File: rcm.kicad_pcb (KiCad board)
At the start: 2 copper layers, 100 x 100 mm, 158 parts, among them Y1 8MHz, Y2 32.768kHz

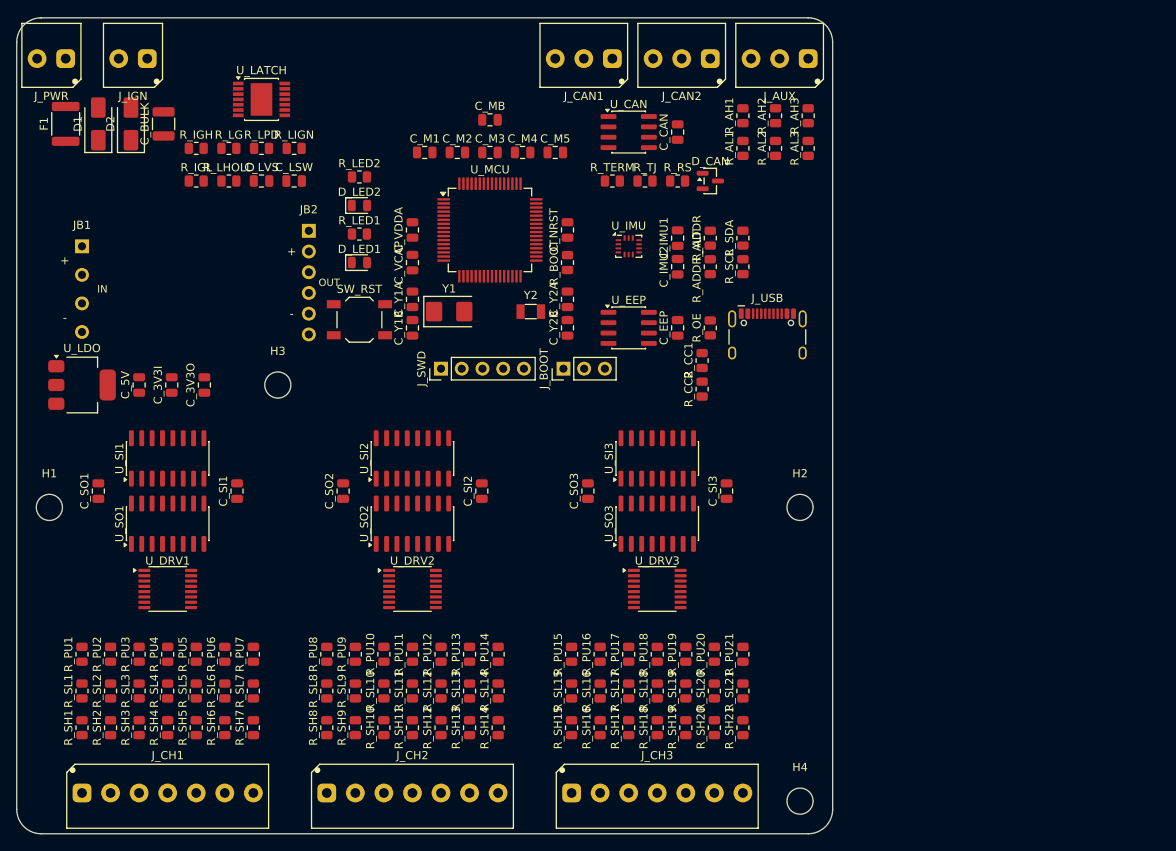
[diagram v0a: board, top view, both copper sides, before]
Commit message: rcm: reshape the board to 140x70 to match the keypad button panel
The panel is 8 momentary switches in 2 rows of 4 at 35mm each, so the board is
now 140 x 70mm. That is 98cm2 against the previous 100 x 100mm draft's 100cm2 -
the same area reshaped rather than a resize, so nothing was traded away for it.

A 70mm-tall board cannot take the old 46mm channel tiles, so each tile's driver,
both shift registers and their decoupling now sit in ONE row instead of a
column: 31mm of tile height, spending the width the wider board has. The north
half was rebuilt across the full 140mm.

Two bugs found on the way, both worth remembering:

- expand_placement pairs members[i] with refs[i]. Reordering the member offsets
  without reordering the ref list put U_SI in C_SO's slot on all three tiles. It
  only surfaced because those two collided; a reorder landing parts somewhere
  legal would have passed every check and still been wrong.
- The buck module body has no courtyard by design, so the placement lint is
  blind to it. gen_plan.py now hard-asserts the area is clear, and that assert
  immediately caught both status LEDs and a resistor underneath the module after
  the reshape - with the lint reporting 0 errors.

Placement lint 0/0, board DRC 0 errors. The 111 remaining warnings are all
silkscreen and get cleaned up in the dedicated pass at the end.

Co-Authored-By: Claude Opus 5 <noreply@anthropic.com>
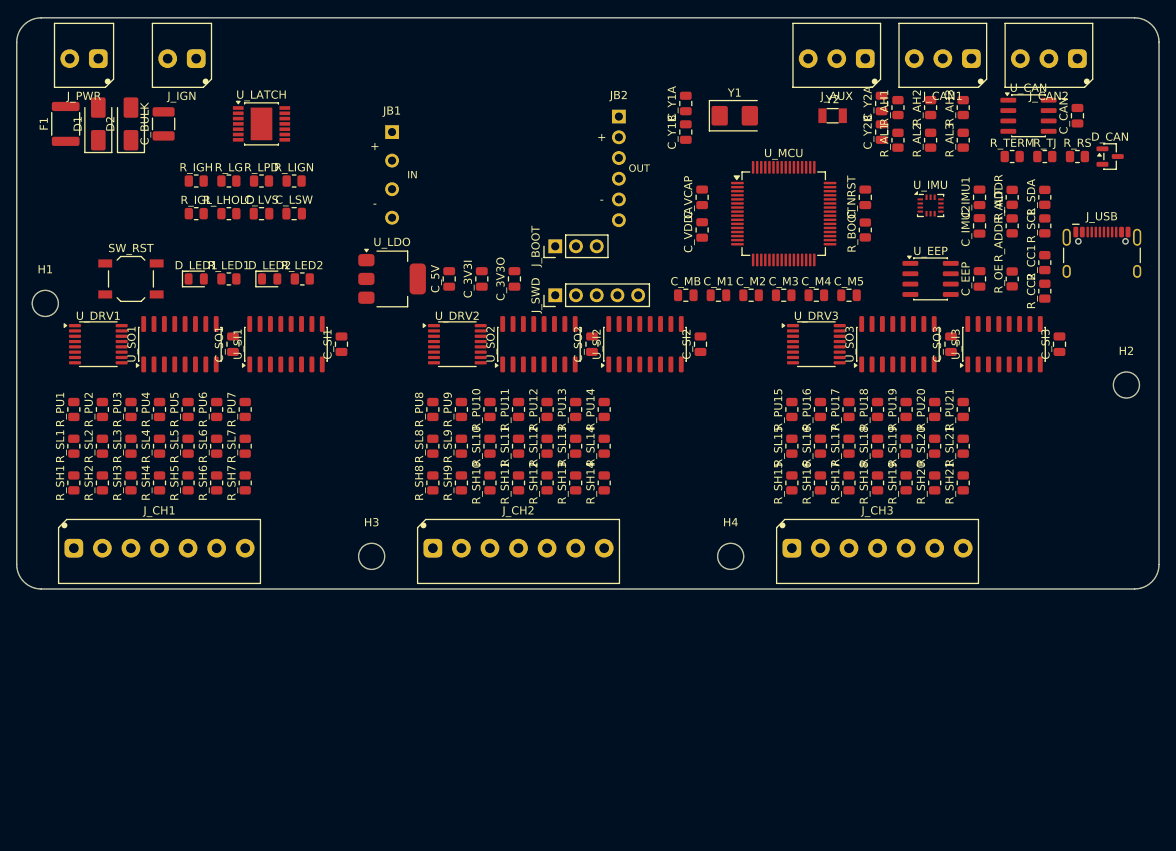
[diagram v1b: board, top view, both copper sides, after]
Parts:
- moved D_CAN 49.1 mm to (134.0, 17.0)
- moved R_RS 49.1 mm to (130.0, 17.0)
- moved R_TERM 49.1 mm to (122.0, 17.0)
- moved R_TJ 49.1 mm to (126.0, 17.0)
- moved C_CAN 49.0 mm to (130.0, 12.0)
- moved U_CAN 49.0 mm to (124.0, 12.0)
- moved C_SO3 48.0 mm to (114.5, 40.0)
- moved C_Y2A 45.4 mm to (106.0, 10.5)
- moved C_Y2B 45.4 mm to (106.0, 14.0)
- moved J_CAN2 45.0 mm to (130.0, 5.00)
- moved U_SI3 44.7 mm to (121.0, 40.0)
- moved C_SI3 44.6 mm to (127.8, 40.0)
- moved Y2 44.1 mm to (100.0, 12.0)
- moved J_CAN1 44.0 mm to (117.0, 5.00)
- moved R_CC1 43.7 mm to (126.0, 30.0)
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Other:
- board size 100 x 100 mm -> 140 x 70 mm

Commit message: rcm: reverse the 595 data chain and give the mounting holes washer clearance
Reviewing the rendered board, the shift-register data line entered at the tile
FURTHEST from the MCU - a ~74mm haul across the board before the chain doubled
back east past the MCU. Reversed so it enters at the nearest tile and ripples
away. Sets the bit order: first byte out lands in U_SO1 (channels 1-7).

The four mounting holes all sat 3.5-4.0mm from a board edge, which is exactly
the radius of an M3 washer - it would have overhung. Moved to 5mm+ and lifted
the two bottom holes clear of the terminal-block row.

Schematic ERC 0 and round-trip MATCH; placement lint 0/0; board DRC 0 errors.

Co-Authored-By: Claude Opus 5 <noreply@anthropic.com>
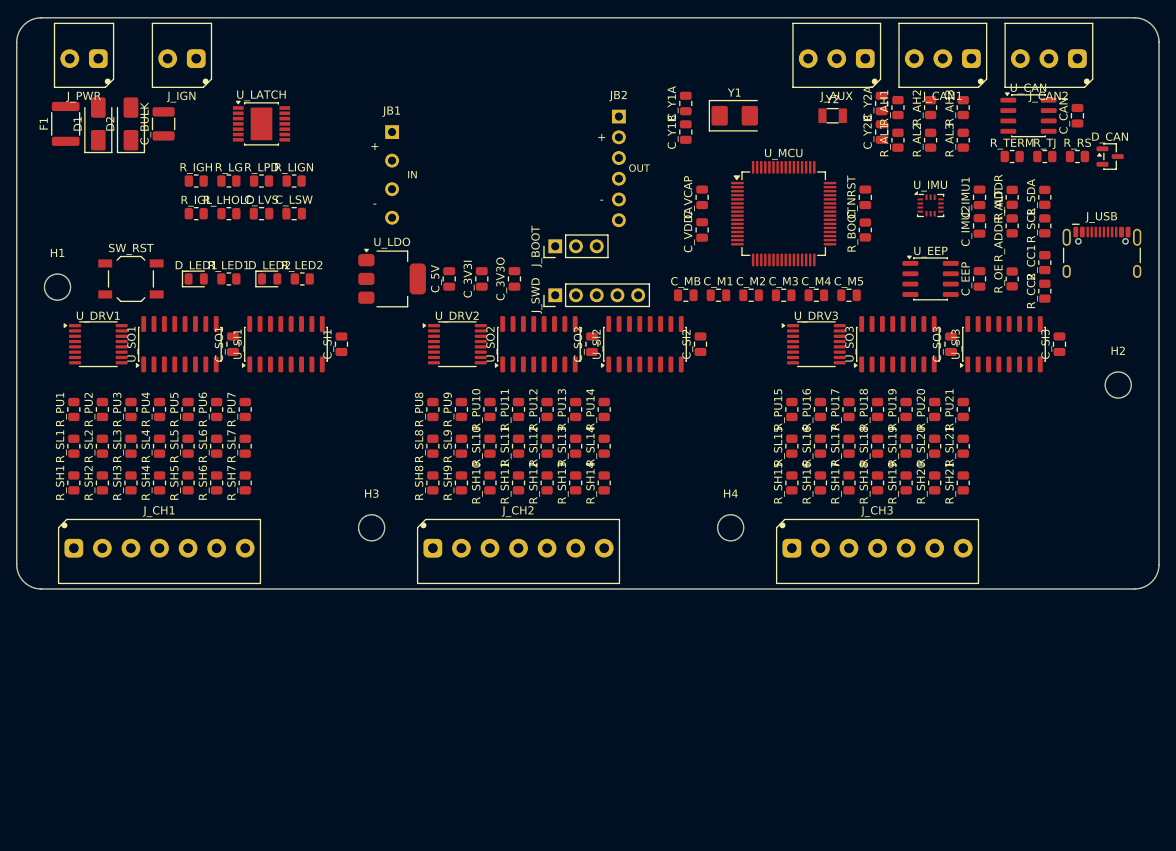
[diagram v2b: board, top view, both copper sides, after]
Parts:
- moved H3 3.50 mm to (43.5, 62.5)
- moved H4 3.50 mm to (87.5, 62.5)
- moved H1 2.50 mm to (5.00, 33.0)
- moved H2 1.00 mm to (135.0, 45.0)
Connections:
- U_SO1 pad 14: SR_MOSI -> SR_CH21
- U_SO1 pad 9: SR_CH12 -> unconnected-(U_SO1-QH'-Pad9)
- U_SO2 pad 14: SR_CH12 -> SR_CH32
- U_SO2 pad 9: SR_CH23 -> SR_CH21
- U_SO3 pad 14: SR_CH23 -> SR_MOSI
- U_SO3 pad 9: unconnected-(U_SO3-QH'-Pad9) -> SR_CH32

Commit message: rcm: centre the connectors, corner the mounting holes, registers beside resistors
Three layout changes from reviewing the rendered board:

- Both terminal groups are now centred on their edge instead of bunched toward
  the ends, which is what freed the corners.
- The four mounting holes moved to the corners, 5mm clear of the edge.
- Each tile's driver and both shift registers now sit BESIDE the resistor block
  rather than in a row above it. The registers are what those resistors talk to,
  so they are next to their own signals instead of a tile-width away.

The members/refs pairing bug bit a second time during this rework - reordering
the tile offsets without reordering the ref list put U_SI in C_SO's slot on all
three tiles. Fixed structurally: the tile is now a list of
(dx, dy, rot, ref-template) tuples with both lists derived from it, so an offset
and its ref cannot drift apart. Relying on two hand-maintained lists staying in
sync was the actual defect, not the two times I got it wrong.

Placement lint 0/0, board DRC 0 errors.

Co-Authored-By: Claude Opus 5 <noreply@anthropic.com>
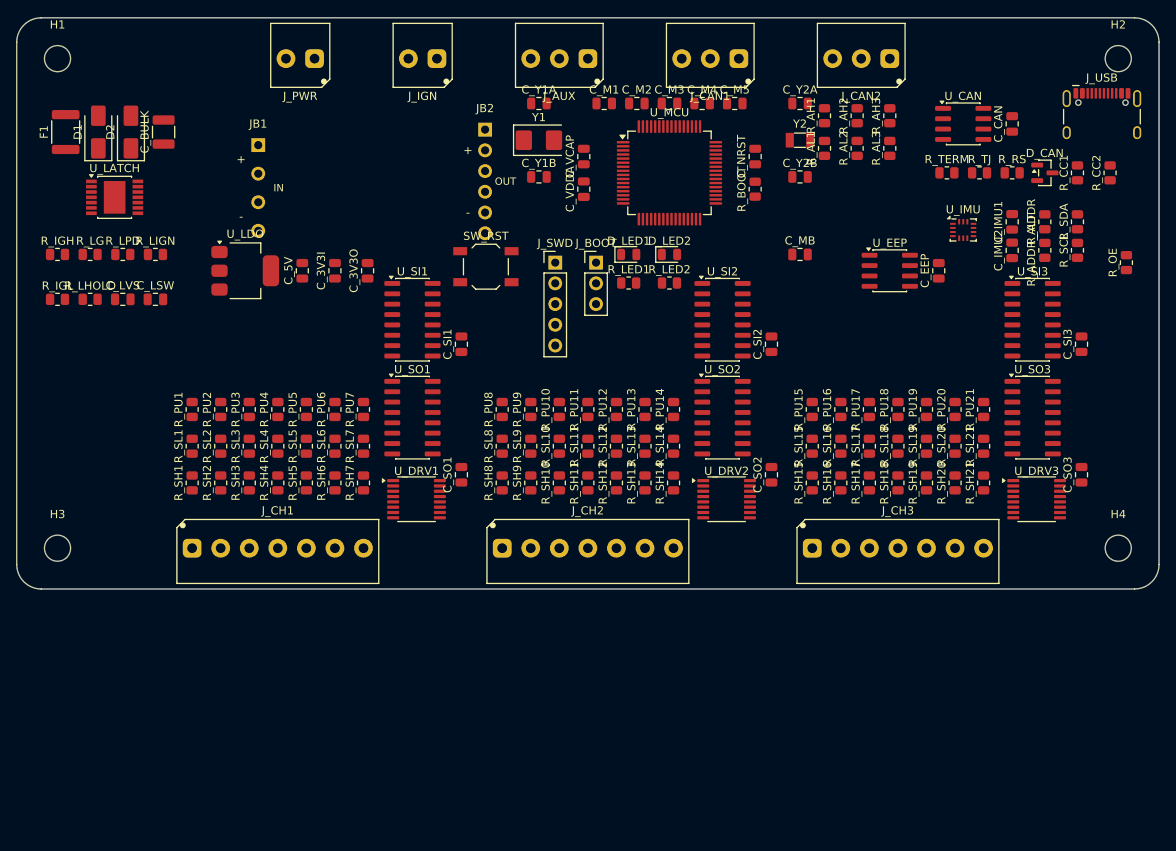
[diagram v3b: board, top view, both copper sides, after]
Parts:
- moved D_LED1 53.1 mm to (75.0, 29.0)
- moved D_LED2 49.1 mm to (80.0, 29.0)
- moved R_LED1 49.0 mm to (75.0, 32.5)
- moved H4 47.6 mm to (135.0, 65.0)
- moved R_LED2 45.0 mm to (80.0, 32.5)
- moved SW_RST 43.5 mm to (57.5, 30.5)
- moved U_DRV1 43.4 mm to (49.0, 59.0)
- moved H2 40.0 mm to (135.0, 5.00)
- moved H3 38.6 mm to (5.00, 65.0)
- moved U_DRV2 38.1 mm to (87.0, 59.0)
- moved J_AUX 34.0 mm to (70.0, 5.00)
- moved U_DRV3 33.0 mm to (125.0, 59.0)
- moved C_SO1 32.2 mm to (54.5, 56.0)
- moved U_SO1 29.9 mm to (48.5, 49.0), turned to 0 degrees
- moved J_IGN 29.5 mm to (51.5, 5.00)
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
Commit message: rcm: registers back north of the resistors, everything spread along the length
Walks back the beside-the-resistors arrangement. The driver and both shift
registers are in a row north of the resistor block again, and the channel
columns now use a 6.0mm pitch - wider than the terminal's 3.5mm poles - so the
resistor rows and the registers above them spread evenly along the board instead
of bunching into tight clusters with dead space between them. That extra spacing
is also routing room. About 8mm of margin is left at each end.

Terminals stay centred on their edges and the mounting holes stay in the
corners.

Placement lint 0/0, board DRC 0 errors.

Note to self: read the DRC output, not just the report file - a stale JSON from a
previous run had me chasing a short between two parts that were 12mm apart on the
actual board.

Co-Authored-By: Claude Opus 5 <noreply@anthropic.com>
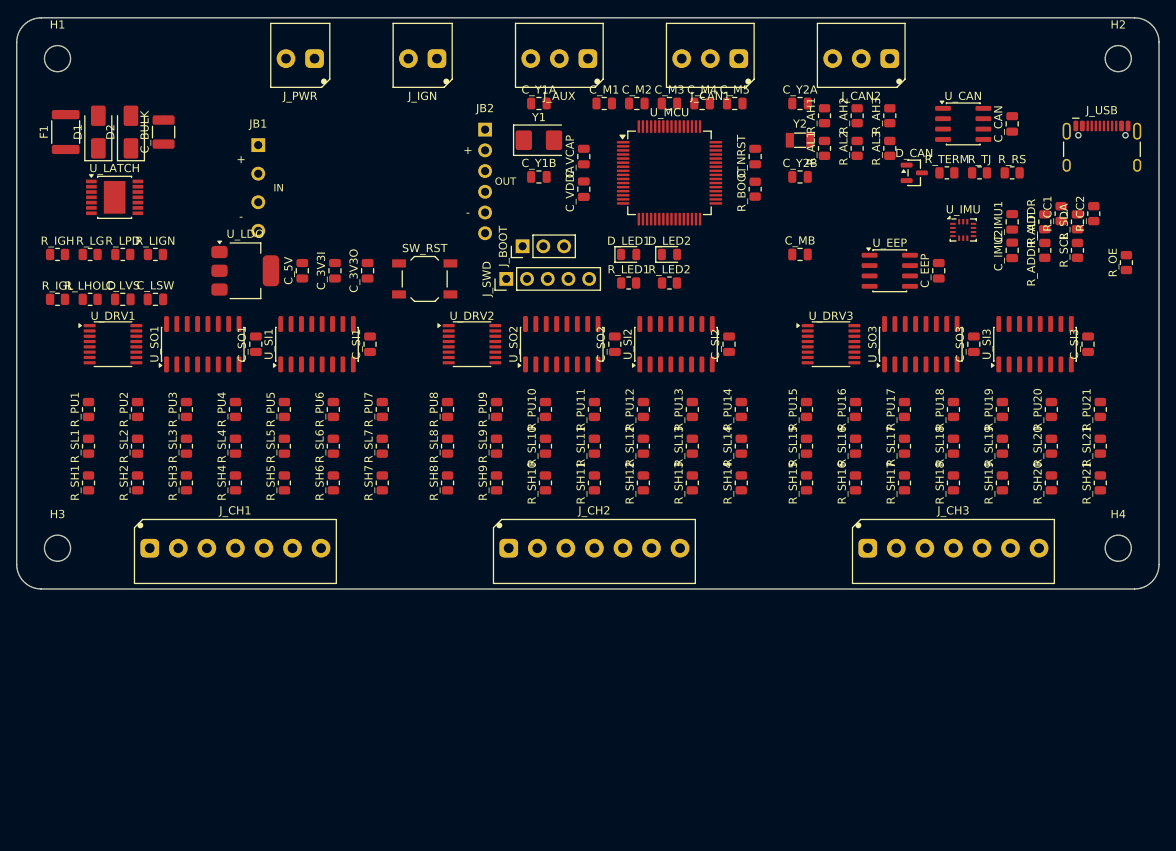
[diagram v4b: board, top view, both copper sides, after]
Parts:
- moved U_DRV1 41.8 mm to (11.8, 40.0)
- moved U_DRV2 36.5 mm to (55.8, 40.0)
- moved U_DRV3 31.6 mm to (99.8, 40.0)
- moved C_SO1 29.9 mm to (29.3, 40.0)
- moved U_SO1 27.2 mm to (22.8, 40.0), turned to 90 degrees
- moved C_SO2 25.0 mm to (73.3, 40.0)
- moved U_SO2 21.7 mm to (66.8, 40.0), turned to 90 degrees
- moved C_SO3 20.7 mm to (117.3, 40.0)
- moved U_SO3 16.4 mm to (110.8, 40.0), turned to 90 degrees
- moved D_CAN 16.0 mm to (110.0, 19.0)
- moved R_PU21 14.3 mm to (132.8, 48.0)
- moved R_SH21 14.3 mm to (132.8, 57.0)
- moved R_SL21 14.3 mm to (132.8, 52.5)
- moved R_PU1 12.7 mm to (8.80, 48.0)
- moved R_SH1 12.7 mm to (8.80, 57.0)
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
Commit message: rcm: move the status LEDs beside PWR_IN, and settle the mounting holes
LEDs relocated to the north edge next to J_PWR per the user, who notes they will
likely be covered anyway.

Mounting holes stay in the corners: the button panel is being 3D-printed after
this board and made to suit it, so the board drives the panel's fixing pattern
rather than waiting on an enclosure constraint. That closes the last open
placement question.

Placement lint 0/0, board DRC 0 errors.

Co-Authored-By: Claude Opus 5 <noreply@anthropic.com>
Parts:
- moved D_LED1 57.3 mm to (23.0, 5.00)
- moved D_LED2 57.3 mm to (28.0, 5.00)
- moved R_LED1 57.1 mm to (23.0, 9.00)
- moved R_LED2 57.1 mm to (28.0, 9.00)
